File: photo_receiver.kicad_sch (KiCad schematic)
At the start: 7 parts

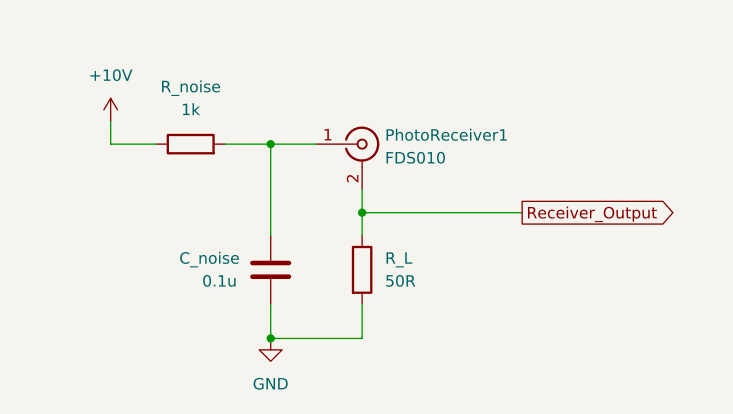
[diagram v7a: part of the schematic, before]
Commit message: Changed receiver load resistor
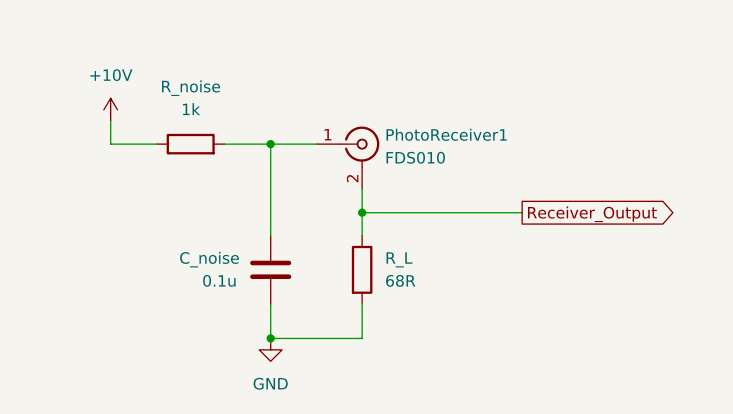
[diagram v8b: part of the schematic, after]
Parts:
- R_L: value 50R -> 68R
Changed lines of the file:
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@@
       (effects (font (size 1.27 1.27)) (justify left))
     )
-    (property "Value" "50R" (id 1) (at 144.78 106.6799 0)
+    (property "Value" "68R" (id 1) (at 144.78 106.6799 0)
       (effects (font (size 1.27 1.27)) (justify left))
     )
